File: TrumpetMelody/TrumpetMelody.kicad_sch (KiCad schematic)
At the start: 79 parts, among them J1 USB_B_Micro, J2 Conn_01x05, J3 640456-3, J4 640456-3, SW1 SW_Push, U1 STM32F411RETx, U2 TLV62565DBVR, U3 MAX98357AETE_T, U4 MAX7375AXR805

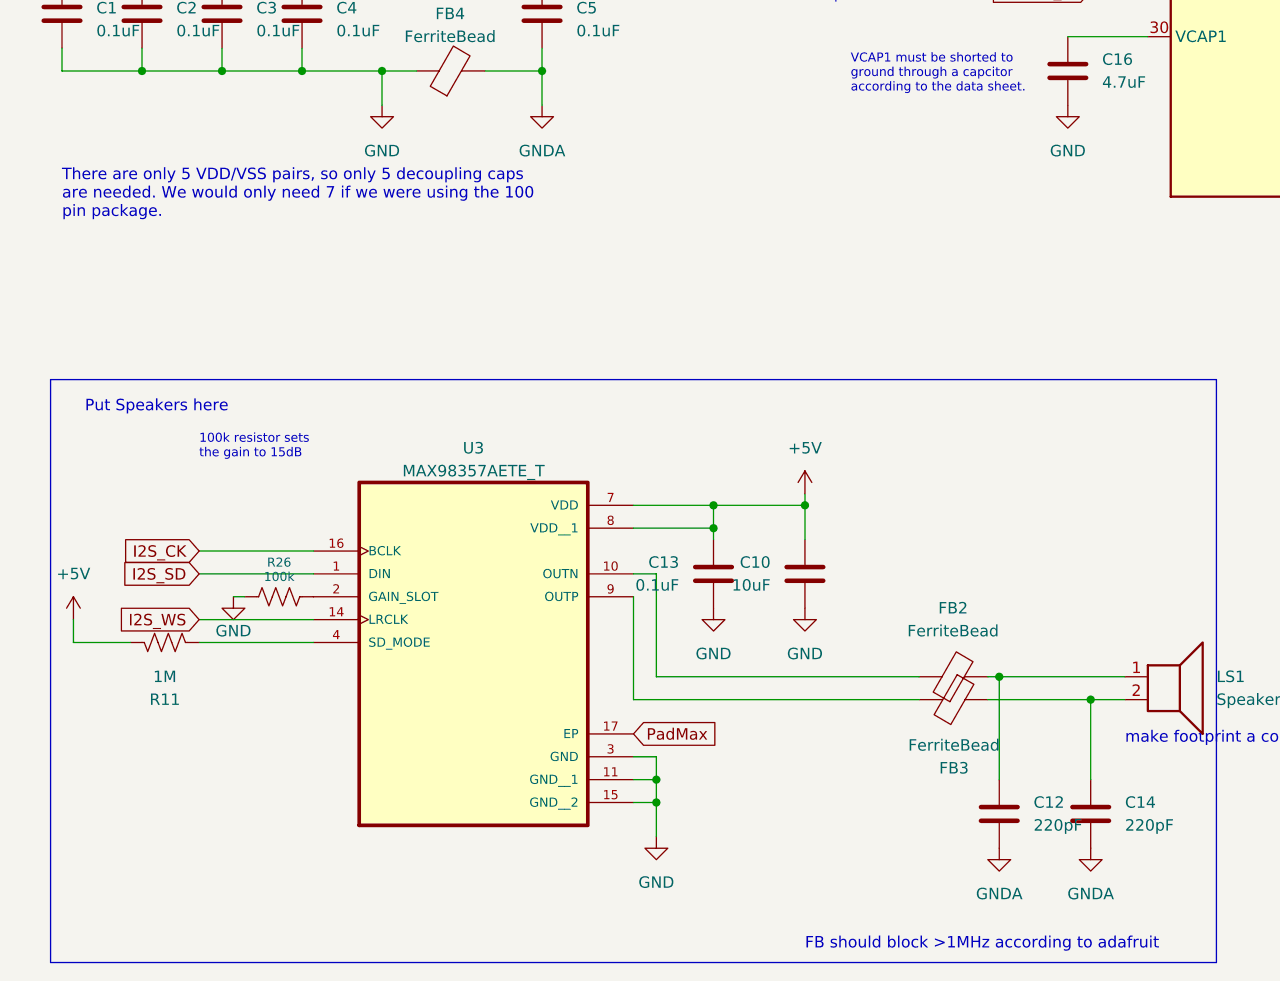
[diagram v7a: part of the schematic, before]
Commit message: Added FB to simplify AGND
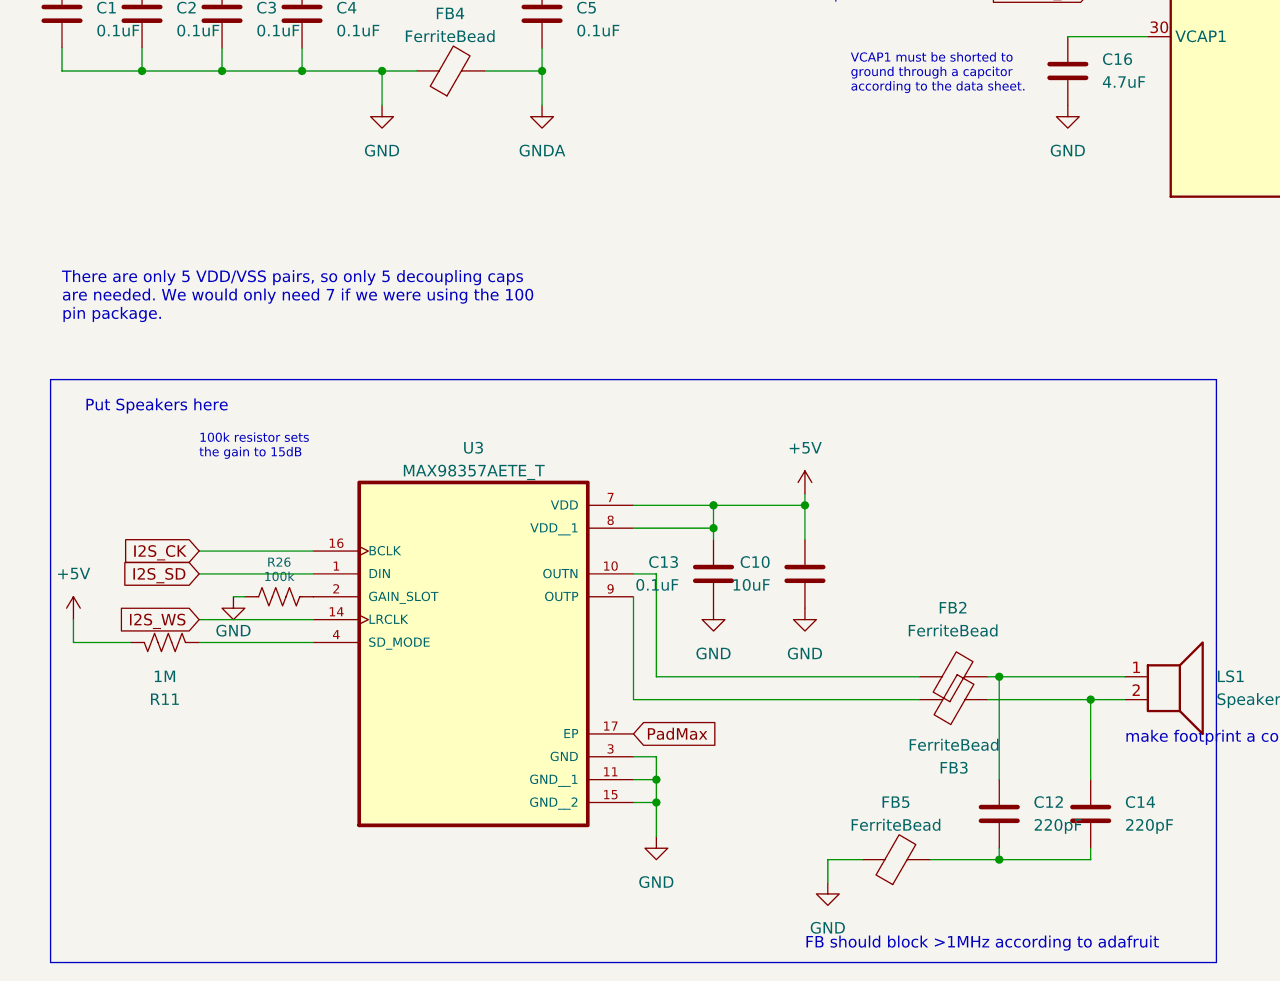
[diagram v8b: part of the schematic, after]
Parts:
- added FB5: FerriteBead, TrumpetMelodyFootprintLibrary:FB_LI0805G201R-10, symbol Device:FerriteBead
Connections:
- net GND: now also FB5.1
- net GNDA: no longer C12.2, C14.2
- new net: C12.2, C14.2, FB5.2
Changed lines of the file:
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@@
   (junction (at 77.47 27.94) (diameter 0) (color 0 0 0 0)
   )
+  (junction (at 121.92 262.89) (diameter 0) (color 0 0 0 0)
+  )
   (junction (at 15.24 30.48) (diameter 0) (color 0 0 0 0)
   )
@@
     (stroke (width 0) (type default))
   )
+  (wire (pts (xy 121.92 262.89) (xy 132.08 262.89))
+    (stroke (width 0) (type default))
+  )
   (wire (pts (xy 246.38 53.34) (xy 250.19 53.34))
     (stroke (width 0) (type default))
@@
     (stroke (width 0) (type default))
   )
+  (wire (pts (xy 106.68 262.89) (xy 102.87 262.89))
+    (stroke (width 0) (type default))
+  )
   (wire (pts (xy 39.37 27.94) (xy 46.99 27.94))
     (stroke (width 0) (type default))
@@
     (stroke (width 0) (type default))
   )
+  (wire (pts (xy 114.3 262.89) (xy 121.92 262.89))
+    (stroke (width 0) (type default))
+  )
   (wire (pts (xy 345.44 233.68) (xy 345.44 240.03))
     (stroke (width 0) (type default))
@@
     (stroke (width 0) (type default))
   )
+  (wire (pts (xy 132.08 261.62) (xy 132.08 262.89))
+    (stroke (width 0) (type default))
+  )
   (wire (pts (xy 204.47 234.95) (xy 204.47 240.03))
     (stroke (width 0) (type default))
@@
     (stroke (width 0) (type default))
   )
+  (wire (pts (xy 121.92 262.89) (xy 121.92 261.62))
+    (stroke (width 0) (type default))
+  )
   (wire (pts (xy 77.47 27.94) (xy 81.28 27.94))
     (stroke (width 0) (type default))
@@
     (stroke (width 0) (type default))
   )
+  (wire (pts (xy 102.87 262.89) (xy 102.87 265.43))
+    (stroke (width 0) (type default))
+  )
   (wire (pts (xy 182.88 222.25) (xy 185.42 222.25))
     (stroke (width 0) (type default))
@@
   )
   (text "There are only 5 VDD/VSS pairs, so only 5 decoupling caps\nare needed. We would only need 7 if we were using the 100\npin package."
-    (at 17.78 191.77 0)
+    (at 17.78 203.2 0)
     (effects (font (size 1.27 1.27)) (justify left bottom))
   )
@@
     )
   )
-  (symbol (lib_id "power:GNDA") (at 121.92 261.62 0) (unit 1)
-    (in_bom yes) (on_board yes) (dnp no) (fields_autoplaced)
-    (property "Reference" "#PWR033" (at 121.92 267.97 0)
-      (effects (font (size 1.27 1.27)) hide)
-    )
-    (property "Value" "GNDA" (at 121.92 266.7 0)
-      (effects (font (size 1.27 1.27)))
-    )
-    (property "Footprint" "" (at 121.92 261.62 0)
-      (effects (font (size 1.27 1.27)) hide)
-    )
-    (property "Datasheet" "" (at 121.92 261.62 0)
-      (effects (font (size 1.27 1.27)) hide)
-    )
-    (pin "1")
-    (instances
-      (project "TrumpetMelody"
-        (path "/646bb87a-580f-408c-a344-dec391089cbb"
-          (reference "#PWR033") (unit 1)
-        )
-      )
-    )
-  )
   (symbol (lib_id "power:GNDA") (at 302.26 167.64 0) (unit 1)
     (in_bom yes) (on_board yes) (dnp no) (fields_autoplaced)
@@
     )
   )
+  (symbol (lib_id "power:GND") (at 102.87 265.43 0) (mirror y) (unit 1)
+    (in_bom yes) (on_board yes) (dnp no) (fields_autoplaced)
+    (property "Reference" "#PWR034" (at 102.87 271.78 0)
+      (effects (font (size 1.27 1.27)) hide)
+    )
+    (property "Value" "GND" (at 102.87 270.51 0)
+      (effects (font (size 1.27 1.27)))
+    )
+    (property "Footprint" "" (at 102.87 265.43 0)
+      (effects (font (size 1.27 1.27)) hide)
+    )
+    (property "Datasheet" "" (at 102.87 265.43 0)
+      (effects (font (size 1.27 1.27)) hide)
+    )
+    (pin "1")
+    (instances
+      (project "TrumpetMelody"
+        (path "/646bb87a-580f-408c-a344-dec391089cbb"
+          (reference "#PWR034") (unit 1)
+        )
+      )
+    )
+  )
   (symbol (lib_id "Device:R_US") (at 57.15 48.26 0) (unit 1)
     (in_bom yes) (on_board yes) (dnp no) (fields_autoplaced)
@@
     )
   )
-  (symbol (lib_id "power:GNDA") (at 132.08 261.62 0) (unit 1)
+  (symbol (lib_id "Device:FerriteBead") (at 110.49 262.89 90) (unit 1)
     (in_bom yes) (on_board yes) (dnp no) (fields_autoplaced)
-    (property "Reference" "#PWR034" (at 132.08 267.97 0)
-      (effects (font (size 1.27 1.27)) hide)
+    (property "Reference" "FB5" (at 110.4392 256.54 90)
+      (effects (font (size 1.27 1.27)))
     )
-    (property "Value" "GNDA" (at 132.08 266.7 0)
+    (property "Value" "FerriteBead" (at 110.4392 259.08 90)
       (effects (font (size 1.27 1.27)))
     )
-    (property "Footprint" "" (at 132.08 261.62 0)
+    (property "Footprint" "TrumpetMelodyFootprintLibrary:FB_LI0805G201R-10" (at 110.49 264.668 90)
       (effects (font (size 1.27 1.27)) hide)
     )
-    (property "Datasheet" "" (at 132.08 261.62 0)
+    (property "Datasheet" "~" (at 110.49 262.89 0)
       (effects (font (size 1.27 1.27)) hide)
     )
     (pin "1")
+    (pin "2")
     (instances
       (project "TrumpetMelody"
         (path "/646bb87a-580f-408c-a344-dec391089cbb"
-          (reference "#PWR034") (unit 1)
+          (reference "FB5") (unit 1)
         )
       )
